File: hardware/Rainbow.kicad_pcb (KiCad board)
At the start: 2 copper layers, 63.3 x 47.9 mm, 24 parts, among them J1 PICKit3, J2 UART, J3 BARREL_JACK, J4 HC-05, J5 RGB, Q1 Q_NMOS_GDS, Q2 Q_NMOS_GDS, Q3 Q_NMOS_GDS, SW1 SWITCH, U1 PIC16F15325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

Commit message: Generate gerbers
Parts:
- moved J4 55.6 mm to (169.3, 76.8), turned to 180 degrees
- moved SW1 55.0 mm to (121.1, 103.3), turned to 180 degrees
- moved R4 52.2 mm to (169.2, 82.3), turned to -90 degrees
- moved J2 52.0 mm to (169.0, 93.2), turned to 0 degrees
- moved D2 51.3 mm to (163.8, 71.7), turned to 90 degrees
- moved D1 50.2 mm to (160.6, 106.2), turned to -90 degrees
- moved J3 49.2 mm to (137.6, 111.4), turned to 90 degrees
- moved R1 49.0 mm to (165.4, 98.8), turned to -90 degrees
- moved J5 48.7 mm to (129.4, 67.8), turned to -90 degrees
- moved D4 47.1 mm to (162.1, 102.5), turned to 180 degrees
- moved R3 45.1 mm to (166.0, 90.0), turned to 90 degrees
- moved C2 44.7 mm to (164.2, 78.8), turned to 90 degrees
- moved C3 44.5 mm to (155.9, 106.1), turned to -90 degrees
- moved U1 43.5 mm to (162.1, 99.1), turned to 180 degrees
- moved C1 42.0 mm to (140.0, 66.8), turned to -90 degrees
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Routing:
- net RX: track 42.4 -> 41.0 mm, vias 1 -> 0
- net +5V: track 54.0 -> 53.0 mm
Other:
- board size 63.3 x 47.9 mm -> 63.5 x 48.2 mm

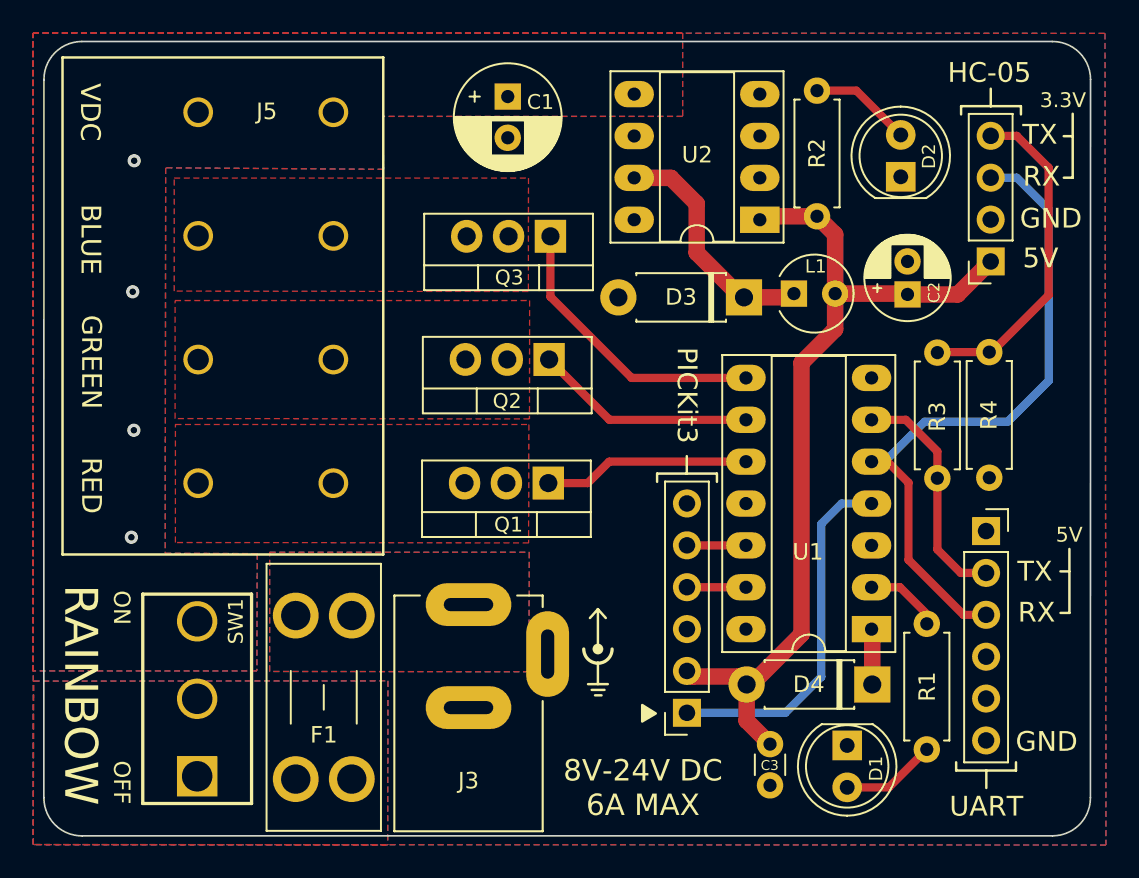
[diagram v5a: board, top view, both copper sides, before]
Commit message: Swap footprints for C1 and C2
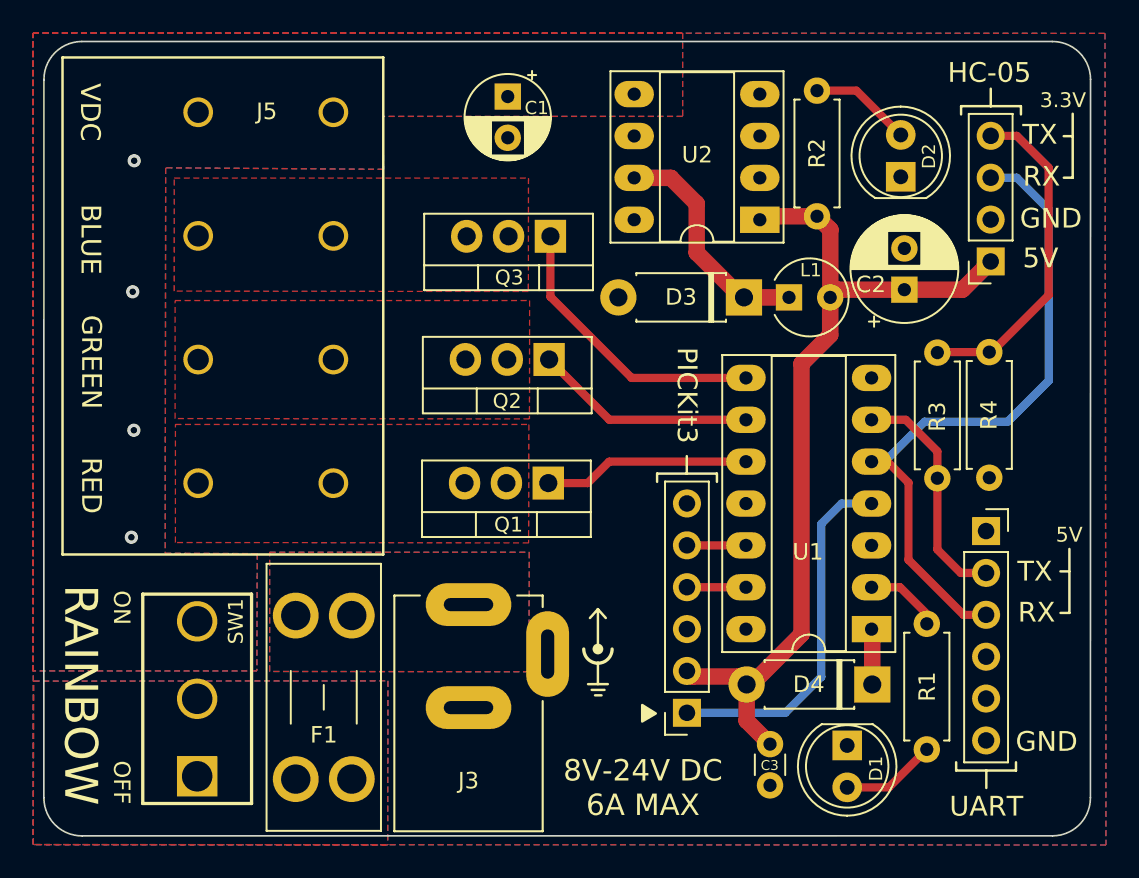
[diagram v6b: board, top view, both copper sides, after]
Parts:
- C1: footprint Capacitor_THT:CP_Radial_D6.3mm_P2.50mm -> Capacitor_THT:CP_Radial_D5.0mm_P2.50mm
- C2: footprint Capacitor_THT:CP_Radial_D5.0mm_P2.00mm -> Capacitor_THT:CP_Radial_D6.3mm_P2.50mm
- moved L1 0.38 mm to (157.0, 79.0)
- moved C2 0.34 mm to (164.0, 78.5)
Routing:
- net RX: track 41.0 -> 40.2 mm
